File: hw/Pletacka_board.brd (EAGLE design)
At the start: 75 x 60 mm, 55 parts, among them U1 LM75BDP-NEW, U2 EL357N(A)(TA)-G, U3 EL357N(A)(TA)-G, U4 EL357N(A)(TA)-G, U5 EL357N(A)(TA)-G, U6 TPS54231D

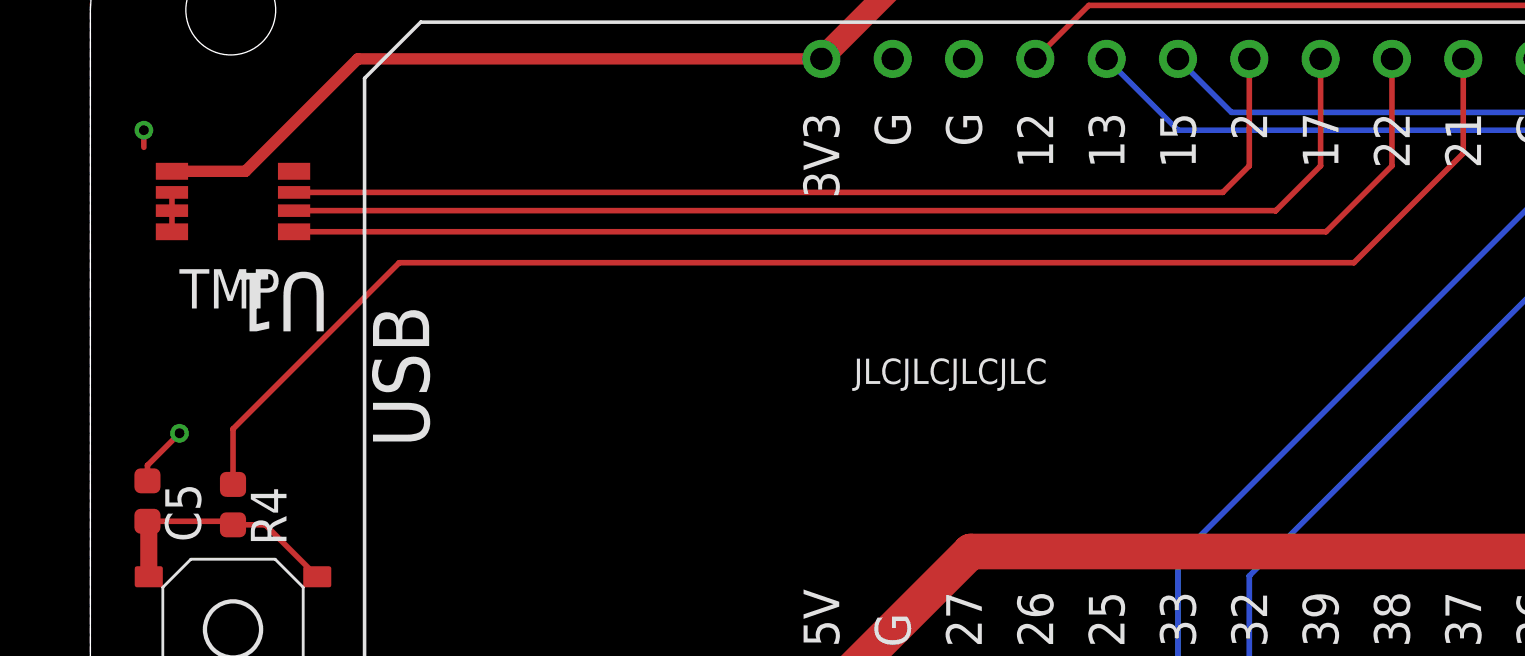
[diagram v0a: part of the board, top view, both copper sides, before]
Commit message: Add pull-up resistors on I2C (close #14)
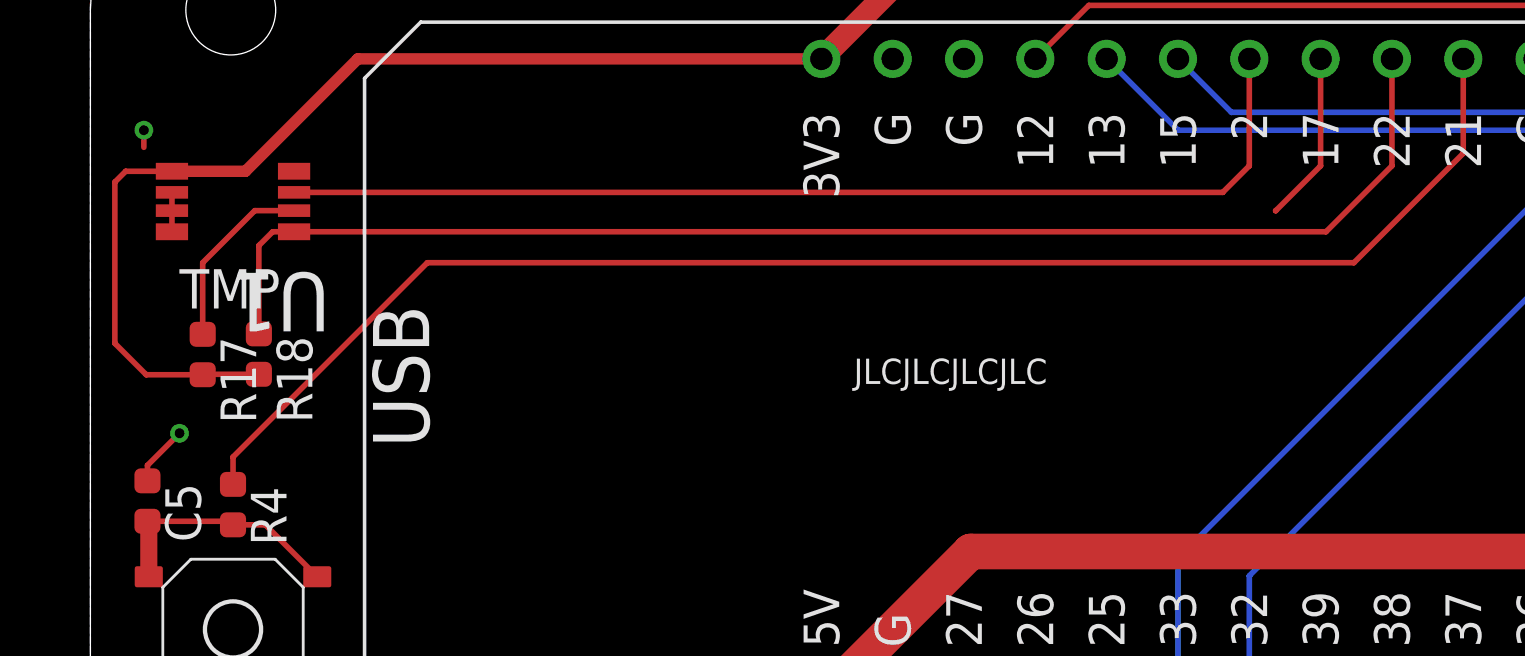
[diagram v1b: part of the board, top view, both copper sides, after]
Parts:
- added R17, R18: 4k7, rcl_upravena:R0603
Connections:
- net +3V3: now also R17.2, R18.2
- net TMP_SCL: now also R17.1
- net TMP_SDA: now also R18.1
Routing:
- net TMP_SCL: track 41.0 -> 12.7 mm
- net +3V3: track 145.8 -> 159.3 mm
- net TMP_SDA: track 43.9 -> 48.5 mm
- net BUTTON1: track 53.3 -> 52.7 mm
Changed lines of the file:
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@@
 <attribute name="VALUE" x="55.5" y="11.5" size="1.27" layer="27" align="top-left"/>
+</element>
+<element name="R17" library="rcl_upravena" package="R0603" value="4k7" x="4" y="42.73" smashed="yes" rot="R270">
+<attribute name="LCSC_ID" value="C23162" x="4" y="42.73" size="1.778" layer="27" rot="R270" display="off"/>
+<attribute name="NAME" x="4.635" y="43.365" size="1.27" layer="25" rot="R270"/>
+<attribute name="VALUE" x="2.095" y="43.365" size="1.27" layer="27" rot="R270"/>
+</element>
+<element name="R18" library="rcl_upravena" package="R0603" value="4k7" x="6" y="42.746" smashed="yes" rot="R270">
+<attribute name="LCSC_ID" value="C23162" x="6" y="42.746" size="1.778" layer="27" rot="R270" display="off"/>
+<attribute name="NAME" x="6.635" y="43.381" size="1.27" layer="25" rot="R270"/>
+<attribute name="VALUE" x="4.095" y="43.381" size="1.27" layer="27" rot="R270"/>
 </element>
 </elements>
@@
 <wire x1="29.4948" y1="56.7198" x2="61.9452" y2="56.7198" width="0.8128" layer="1"/>
 <wire x1="61.9452" y1="56.7198" x2="63.5" y2="55.165" width="0.8128" layer="1"/>
-<wire x1="53.975" y1="30.4" x2="63.5" y2="55.165" width="0" layer="19" extent="1-1"/>
+<contactref element="R17" pad="2"/>
+<contactref element="R18" pad="2"/>
+<wire x1="6" y1="42.026" x2="4.016" y2="42.026" width="0.2" layer="1"/>
+<wire x1="4.016" y1="42.026" x2="4" y2="42.01" width="0.2" layer="1"/>
+<wire x1="4" y1="42.01" x2="1.99" y2="42.01" width="0.2" layer="1"/>
+<wire x1="0.873" y1="43.127" x2="1.99" y2="42.01" width="0.2" layer="1"/>
+<wire x1="2.905" y1="49.257" x2="1.257" y2="49.257" width="0.2" layer="1"/>
+<wire x1="1.257" y1="49.257" x2="0.873" y2="48.873" width="0.2" layer="1"/>
+<wire x1="0.873" y1="48.873" x2="0.873" y2="43.127" width="0.2" layer="1"/>
+<wire x1="13.97" y1="18.695" x2="4.016" y2="42.026" width="0" layer="19" extent="1-1"/>
 </signal>
 <signal name="+5V">
@@
 <wire x1="7.255" y1="47.103" x2="44.008" y2="47.103" width="0.2" layer="1"/>
 <wire x1="44.008" y1="47.103" x2="46.355" y2="49.45" width="0.2" layer="1"/>
+<contactref element="R18" pad="1"/>
+<wire x1="7.255" y1="47.103" x2="6.493" y2="47.103" width="0.2" layer="1"/>
+<wire x1="6.493" y1="47.103" x2="6" y2="46.61" width="0.2" layer="1"/>
+<wire x1="6" y1="46.61" x2="6" y2="43.466" width="0.2" layer="1"/>
 </signal>
 <signal name="TMP_SCL">
-<contactref element="U1" pad="2"/>
 <contactref element="U$1" pad="17"/>
 <wire x1="43.815" y1="53.26" x2="43.815" y2="49.45" width="0.2" layer="1"/>
 <wire x1="42.2148" y1="47.8498" x2="43.815" y2="49.45" width="0.2" layer="1"/>
-<wire x1="7.255" y1="47.855" x2="42.2096" y2="47.855" width="0.2" layer="1"/>
 <wire x1="42.2096" y1="47.855" x2="42.2148" y2="47.8498" width="0.2" layer="1"/>
+<contactref element="R17" pad="1"/>
+<contactref element="U1" pad="2"/>
+<wire x1="7.255" y1="47.855" x2="5.855" y2="47.855" width="0.2" layer="1"/>
+<wire x1="4" y1="46" x2="4" y2="43.45" width="0.2" layer="1"/>
+<wire x1="5.855" y1="47.855" x2="4" y2="46" width="0.2" layer="1"/>
+<wire x1="7.255" y1="47.855" x2="42.2096" y2="47.855" width="0" layer="19" extent="1-1"/>
 </signal>
 <signal name="TMP_OS">
@@
 <wire x1="48.895" y1="53.26" x2="48.895" y2="49.895" width="0.2" layer="1"/>
 <wire x1="48.895" y1="49.895" x2="45" y2="46" width="0.2" layer="1"/>
-<wire x1="45" y1="46" x2="11" y2="46" width="0.2" layer="1"/>
-<wire x1="11" y1="46" x2="5.08" y2="40.08" width="0.2" layer="1"/>
-<wire x1="5.08" y1="40.08" x2="5.08" y2="38.105" width="0.2" layer="1"/>
+<wire x1="45" y1="46" x2="12" y2="46" width="0.2" layer="1"/>
+<wire x1="12" y1="46" x2="5.08" y2="39.08" width="0.2" layer="1"/>
+<wire x1="5.08" y1="39.08" x2="5.08" y2="38.105" width="0.2" layer="1"/>
 </signal>
 <signal name="BUTTON2">

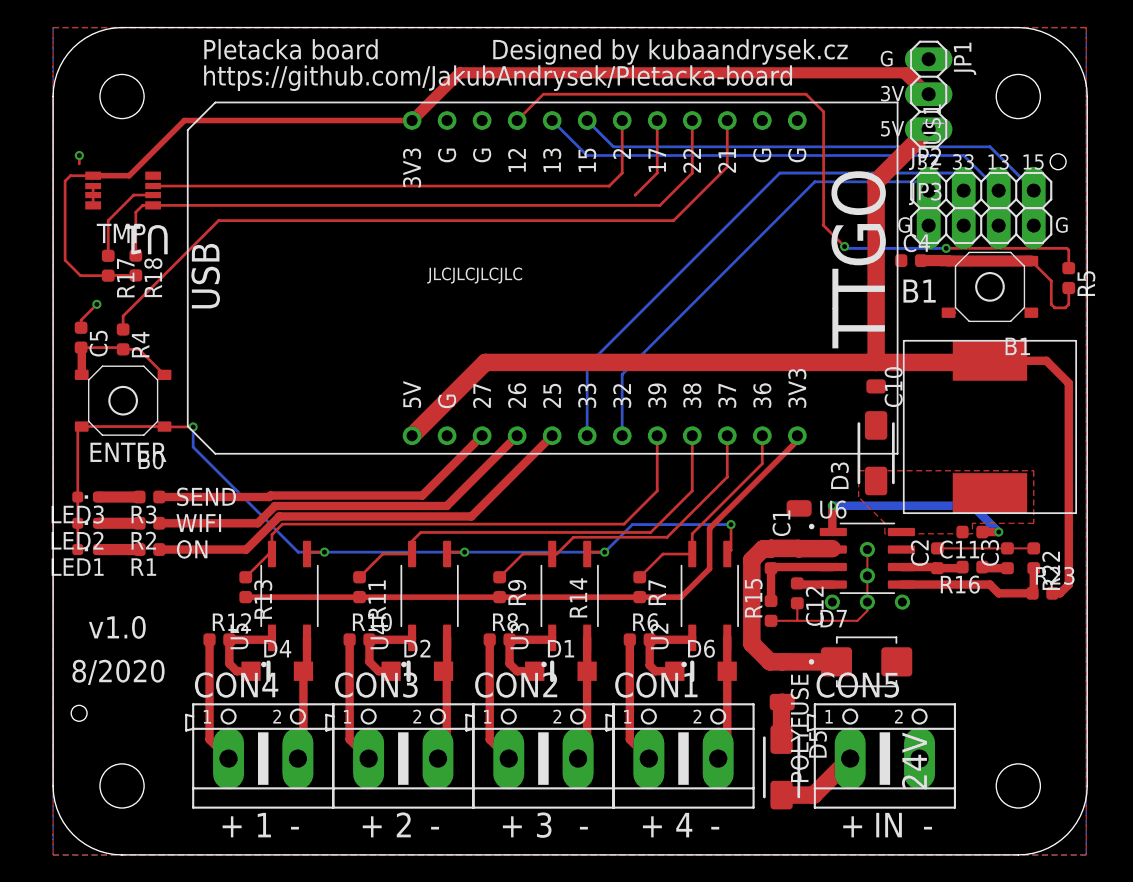
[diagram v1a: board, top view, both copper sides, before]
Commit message: Add input power voltage mesurement
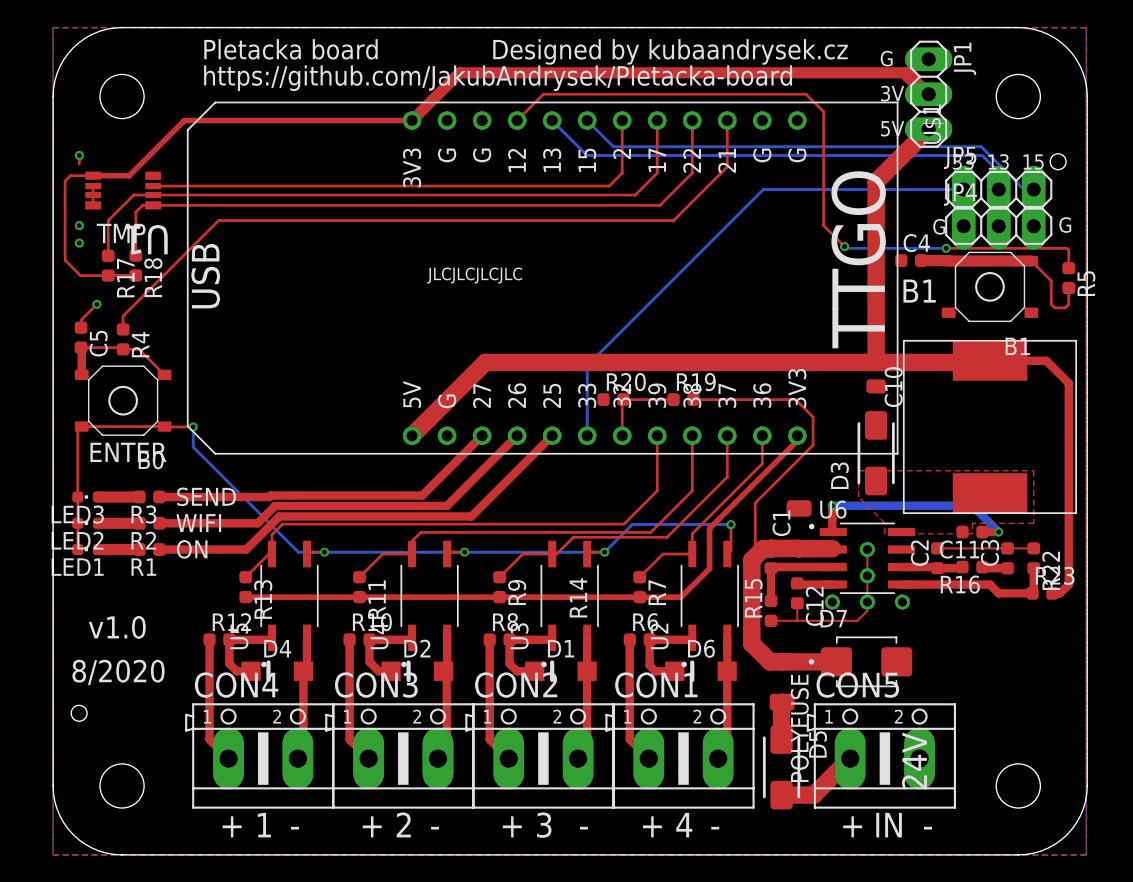
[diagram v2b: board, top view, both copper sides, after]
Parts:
- removed JP2, JP3: (no value), pinhead:1X04
- added JP4, JP5: (no value), pinhead:1X03
- added R19: 36k, rcl_upravena:R0603
- added R20: 1k2, rcl_upravena:R0603
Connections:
- removed net GPIO32: JP2.1, U$1.32
- removed net VIN: C1.1, D7.C, POLYFUSE.1, R14.2, U6.2
- new net +24V: C1.1, D7.C, POLYFUSE.1, R14.2, R19.2, U6.2
- new net PWR_VOLTAGE: R19.1, R20.2, U$1.32
- net GND: now also JP4.1, JP4.2, JP4.3, R20.1; no longer JP3.1, JP3.2, JP3.3, JP3.4
- net GPIO13: now also JP5.2; no longer JP2.3
- net GPIO15: now also JP5.3; no longer JP2.4
- net GPIO33: now also JP5.1; no longer JP2.2
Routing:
- net +24V: track 0.00 -> 43.1 mm
- net TMP_SCL: track 12.7 -> 47.6 mm
- net GPIO32: track 32.7 -> 0.00 mm
- net VIN: track 21.7 -> 0.00 mm
- net PWR_VOLTAGE: track 0.00 -> 6.30 mm
- net GPIO33: track 39.1 -> 37.7 mm
- net GPIO13: track 34.5 -> 35.2 mm
- net LED_ON: track 32.6 -> 31.9 mm
- net GND: vias 12 -> 14
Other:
- board text removed: "32"

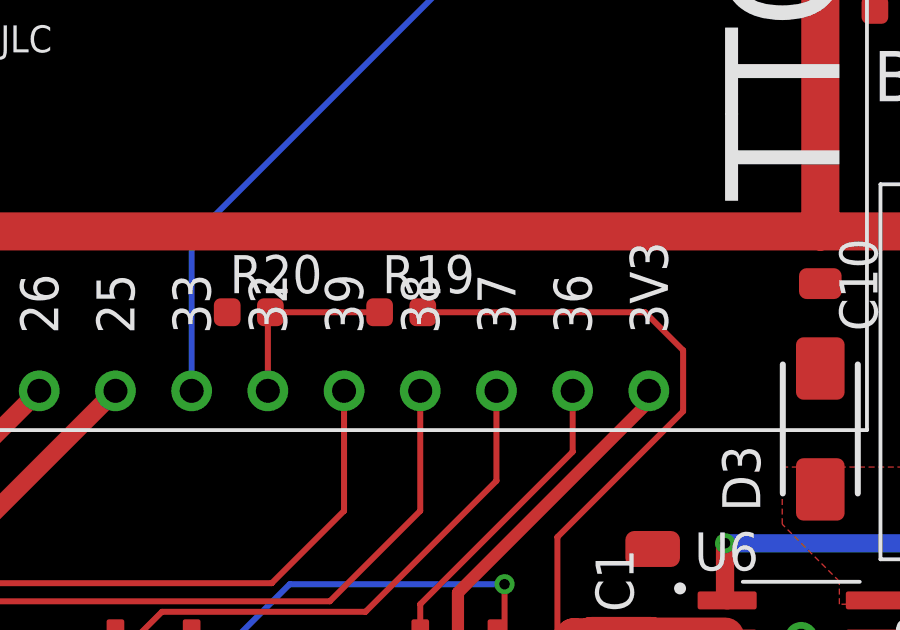
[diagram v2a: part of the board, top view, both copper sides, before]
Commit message: Move voltage mesurement resistors
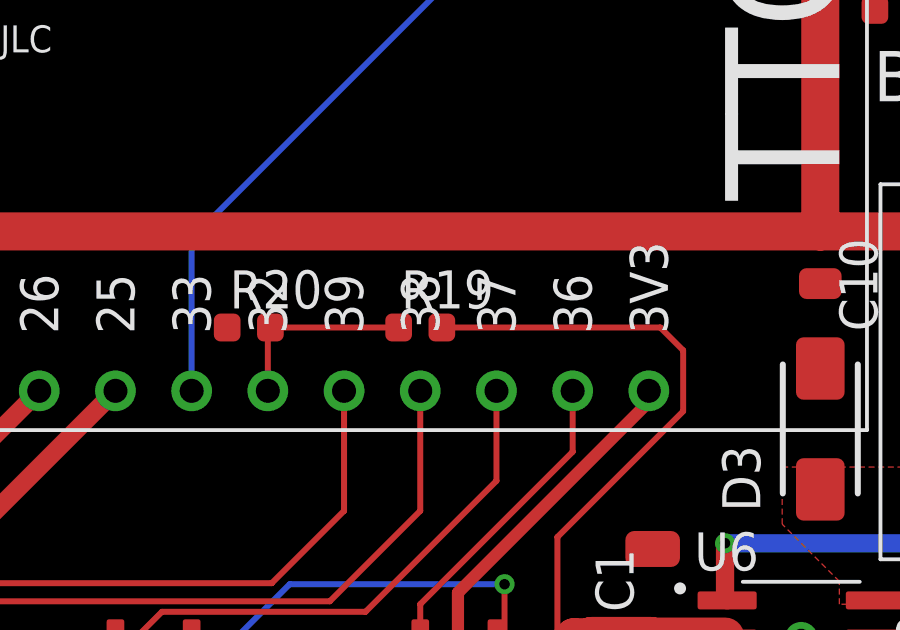
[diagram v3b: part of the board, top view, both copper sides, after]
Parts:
- moved R19 0.81 mm to (46.4, 32.5)
- moved R20 0.51 mm to (40.6, 32.5)
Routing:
- net +24V: track 43.1 -> 42.3 mm
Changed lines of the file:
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@@
 <drawing>
 <settings>
-<setting alwaysvectorfont="no"/>
+<setting alwaysvectorfont="yes"/>
 <setting verticaltext="up"/>
 </settings>
@@
 <attribute name="VALUE" x="64.77" y="45.085" size="1.27" layer="27"/>
 </element>
-<element name="R20" library="rcl_upravena" package="R0603" value="1k2" x="40.64" y="33.02" smashed="yes">
-<attribute name="LCSC_ID" value="C22765" x="40.64" y="33.02" size="1.778" layer="27" display="off"/>
-<attribute name="NAME" x="40.005" y="33.655" size="1.27" layer="25"/>
-<attribute name="VALUE" x="40.005" y="31.115" size="1.27" layer="27"/>
-</element>
-<element name="R19" library="rcl_upravena" package="R0603" value="36k" x="45.72" y="33.02" smashed="yes">
-<attribute name="LCSC_ID" value="C23147" x="45.72" y="33.02" size="1.778" layer="27" display="off"/>
-<attribute name="NAME" x="45.085" y="33.655" size="1.27" layer="25"/>
-<attribute name="VALUE" x="45.085" y="31.115" size="1.27" layer="27"/>
+<element name="R20" library="rcl_upravena" package="R0603" value="1k2" x="40.64" y="32.512" smashed="yes">
+<attribute name="LCSC_ID" value="C22765" x="40.64" y="32.512" size="1.778" layer="27" display="off"/>
+<attribute name="NAME" x="40.005" y="33.147" size="1.27" layer="25"/>
+<attribute name="VALUE" x="40.005" y="30.607" size="1.27" layer="27"/>
+</element>
+<element name="R19" library="rcl_upravena" package="R0603" value="36k" x="46.355" y="32.512" smashed="yes">
+<attribute name="LCSC_ID" value="C23147" x="46.355" y="32.512" size="1.778" layer="27" display="off"/>
+<attribute name="NAME" x="45.72" y="33.147" size="1.27" layer="25"/>
+<attribute name="VALUE" x="45.72" y="30.607" size="1.27" layer="27"/>
 </element>
 </elements>
@@
 <contactref element="R20" pad="2"/>
 <contactref element="R19" pad="1"/>
-<wire x1="41.36" y1="33.02" x2="45" y2="33.02" width="0.2" layer="1"/>
-<wire x1="41.275" y1="30.4" x2="41.275" y2="32.935" width="0.2" layer="1"/>
-<wire x1="41.275" y1="32.935" x2="41.36" y2="33.02" width="0.2" layer="1"/>
+<wire x1="45.635" y1="32.512" x2="41.36" y2="32.512" width="0.2" layer="1"/>
+<wire x1="41.275" y1="30.4" x2="41.275" y2="32.427" width="0.2" layer="1"/>
+<wire x1="41.275" y1="32.427" x2="41.36" y2="32.512" width="0.2" layer="1"/>
 </signal>
 <signal name="+24V">
@@
 <wire x1="55.118" y1="31.75" x2="55.118" y2="29.718" width="0.2" layer="1"/>
 <wire x1="55.118" y1="29.718" x2="50.927" y2="25.527" width="0.2" layer="1"/>
-<wire x1="53.848" y1="33.02" x2="55.118" y2="31.75" width="0.2" layer="1"/>
-<wire x1="46.44" y1="33.02" x2="53.848" y2="33.02" width="0.2" layer="1"/>
+<wire x1="54.356" y1="32.512" x2="55.118" y2="31.75" width="0.2" layer="1"/>
+<wire x1="47.075" y1="32.512" x2="54.356" y2="32.512" width="0.2" layer="1"/>
 <wire x1="50.927" y1="21.637" x2="50.673" y2="21.383" width="0.2" layer="1"/>
 <wire x1="50.927" y1="25.527" x2="50.927" y2="21.637" width="0.2" layer="1"/>

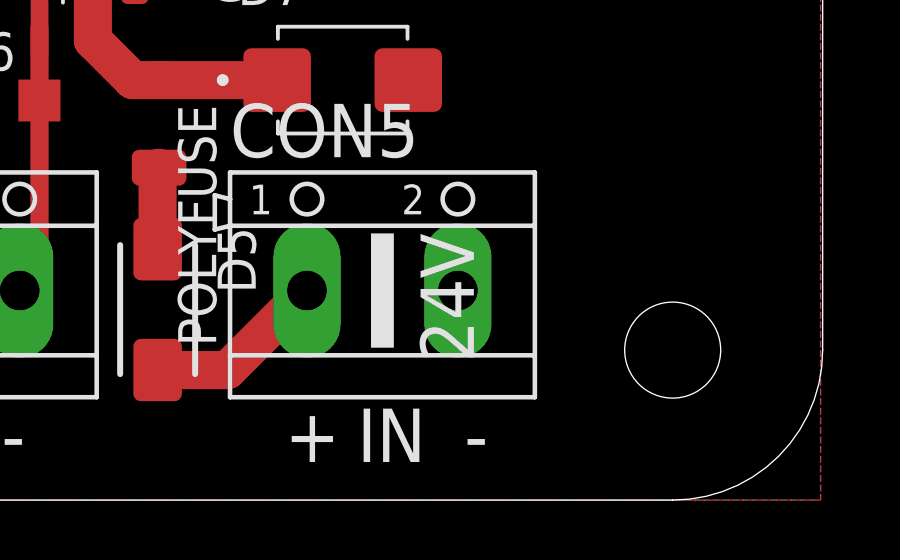
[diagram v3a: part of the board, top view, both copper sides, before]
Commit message: Update resistor R15
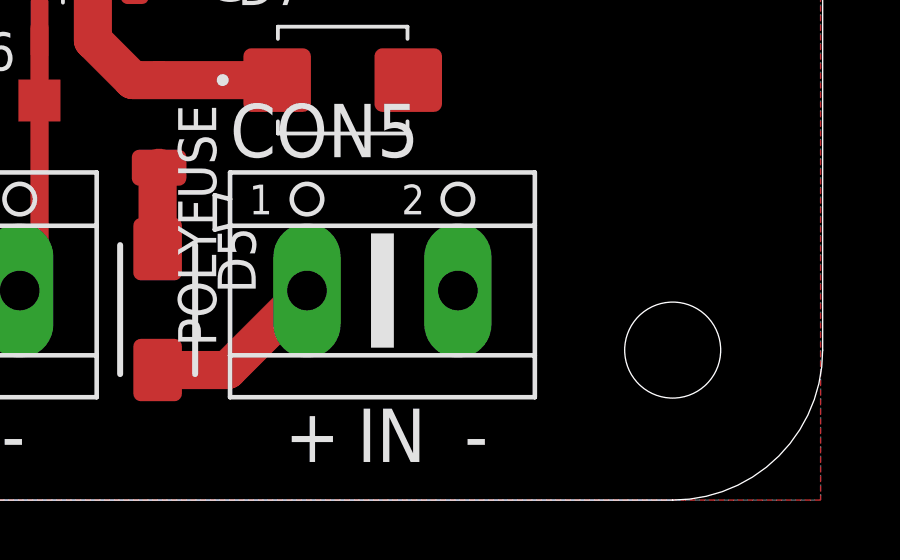
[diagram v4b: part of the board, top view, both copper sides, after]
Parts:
- R15: value 16k -> 33k
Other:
- board text removed: "24V"
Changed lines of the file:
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@@
 <drawing>
 <settings>
-<setting alwaysvectorfont="yes"/>
+<setting alwaysvectorfont="no"/>
 <setting verticaltext="up"/>
 </settings>
@@
 <text x="2.54" y="28.495" size="1.4" layer="21" font="vector" ratio="20">ENTER</text>
 <text x="3.175" y="44.37" size="1.4" layer="21" font="vector" ratio="20">TMP</text>
-<text x="61.595" y="8.89" size="1.778" layer="21" font="vector" ratio="20" rot="R270">24V</text>
 <text x="65.151" y="49.704" size="1.1" layer="21" font="vector" ratio="20">33</text>
 <text x="67.691" y="49.704" size="1.1" layer="21" font="vector" ratio="20">13</text>
@@
 <attribute name="VALUE" x="53.975" y="20.875" size="1.27" layer="27" rot="R90"/>
 </element>
-<element name="R15" library="rcl_upravena" package="R0603" value="16k" x="52.07" y="17.7" smashed="yes" rot="R90">
-<attribute name="LCSC_ID" value="C22818" x="52.07" y="17.7" size="1.778" layer="27" rot="R90" display="off"/>
+<element name="R15" library="rcl_upravena" package="R0603" value="33k" x="52.07" y="17.7" smashed="yes" rot="R90">
+<attribute name="LCSC_ID" value="C4216" x="52.07" y="17.7" size="1.778" layer="27" rot="R90" display="off"/>
 <attribute name="NAME" x="51.435" y="17.065" size="1.27" layer="25" rot="R90"/>
 <attribute name="VALUE" x="53.975" y="17.065" size="1.27" layer="27" rot="R90"/>
